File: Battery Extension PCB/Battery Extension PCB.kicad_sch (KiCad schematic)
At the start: 35 parts, among them P1 Solder_Pad, P10 Solder_Pad, P11 Solder_Pad, P12 Solder_Pad, P13 Solder_Pad, P14 Solder_Pad, P2 Solder_Pad, P3 Solder_Pad, P4 Solder_Pad, P5 Solder_Pad, P6 Solder_Pad, P7 Solder_Pad, P8 Solder_Pad, P9 Solder_Pad, U1 M1250RS-02P, U3 FS8205A, U4 TPS61032PWPR, U5 TP4056, U6 DW01A, U7 FXL0530-6R8-M, U8 AP40P05

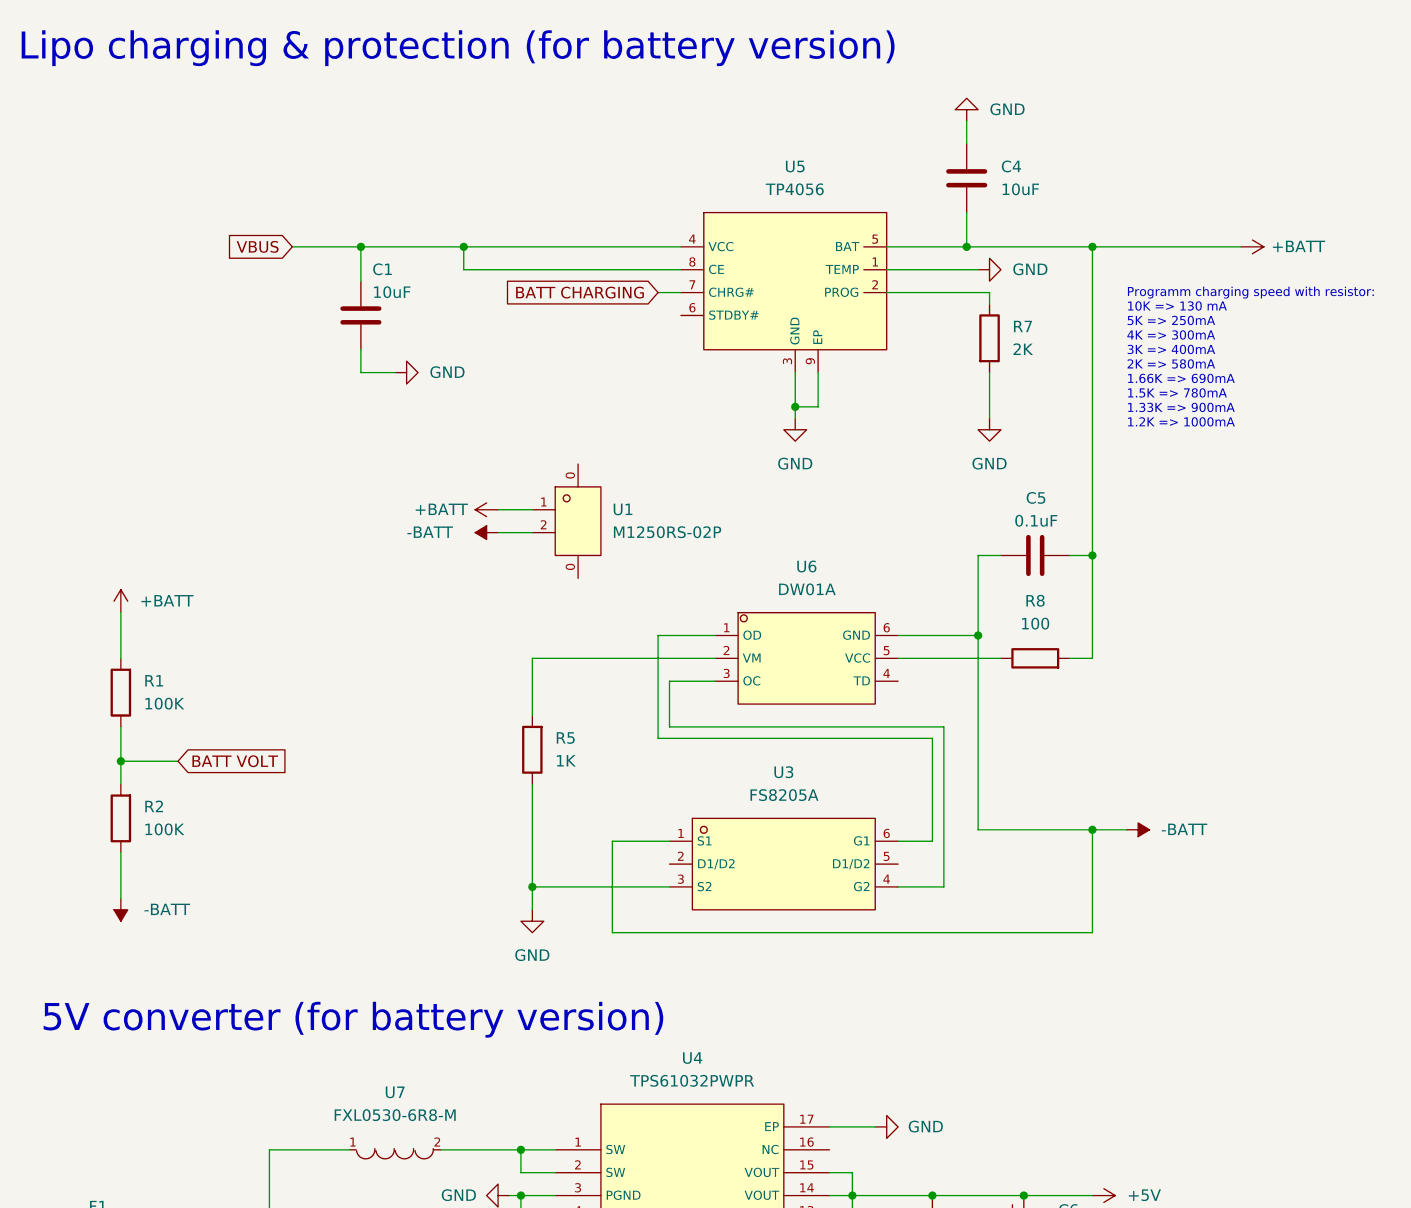
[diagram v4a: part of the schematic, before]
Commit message: fixed schematic naming
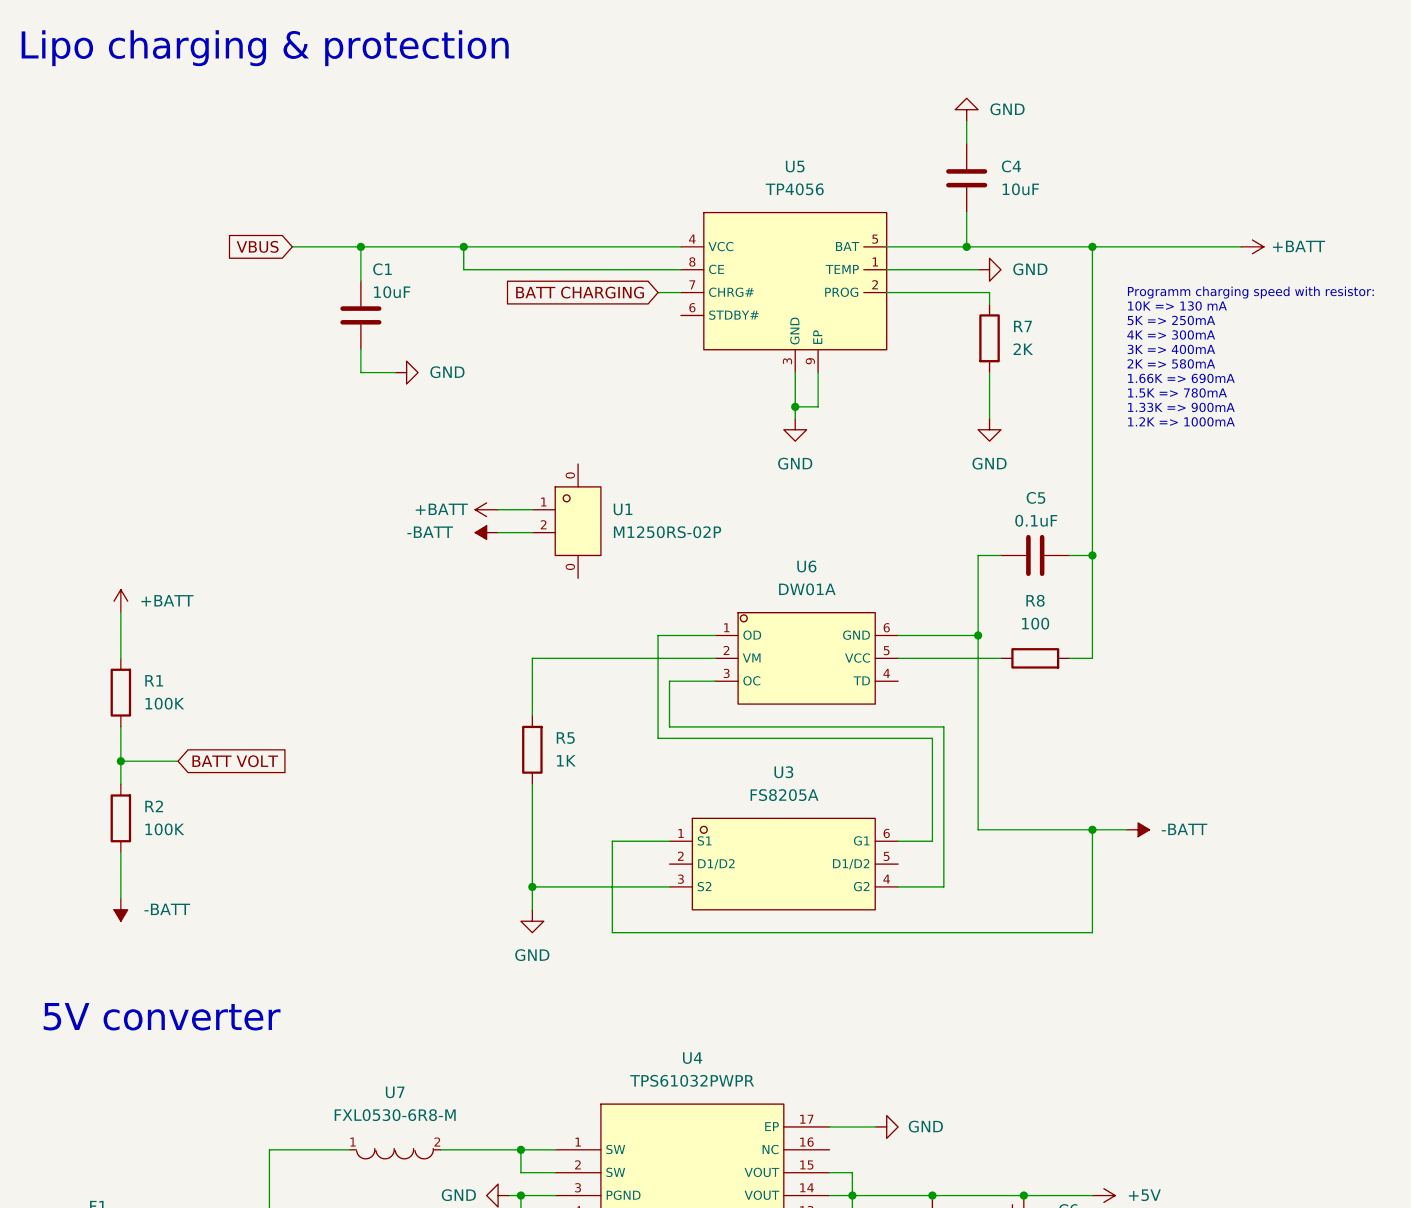
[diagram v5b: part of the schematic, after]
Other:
- note added: "5V converter"
- note added: "Lipo charging & protection"
- note removed: "5V converter (for battery version)"
- note removed: "Lipo charging & protection (for battery version)"
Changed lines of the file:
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@@
     (stroke (width 0) (type default) (color 0 0 0 0))
   )
-  (text "Lipo charging & protection (for battery version)" (at 17.78 21.59 0)
+  (text "Lipo charging & protection" (at 17.78 21.59 0)
     (effects (font (size 3 3)) (justify left bottom))
   )
@@
     (effects (font (size 1 1)) (justify left bottom))
   )
-  (text "5V converter (for battery version)" (at 20.32 129.54 0)
+  (text "5V converter" (at 20.32 129.54 0)
     (effects (font (size 3 3)) (justify left bottom))
   )

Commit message: updated pcb designs
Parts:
- added R3: 100K, Resistor_SMD:R_0402_1005Metric, symbol Device:R
- added U2: AP40P05, footprint:SOT-23-3_L2.9-W1.3-P1.90-LS2.4-BR, symbol MyParts:AP40P05
- R1: value 100K -> 33K; LCSC # C25741 -> C25779
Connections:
- net +BATT: now also U2.2 (S); no longer P1.1, P8.1, U1.1
- net -BATT: now also R3.1
- new net: R3.2, U2.1 (G)
- new net: P1.1, P8.1, U1.1, U2.3 (D)
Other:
- moved on the sheet: P1, P2, P8, P9, U1
